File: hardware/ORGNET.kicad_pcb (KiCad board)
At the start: 2 copper layers, 21 x 50 mm, 3 parts, among them U3 AP2112K-3.3, U5 W25Q128JVP, U6 Raspberry Pi Radio Module 2

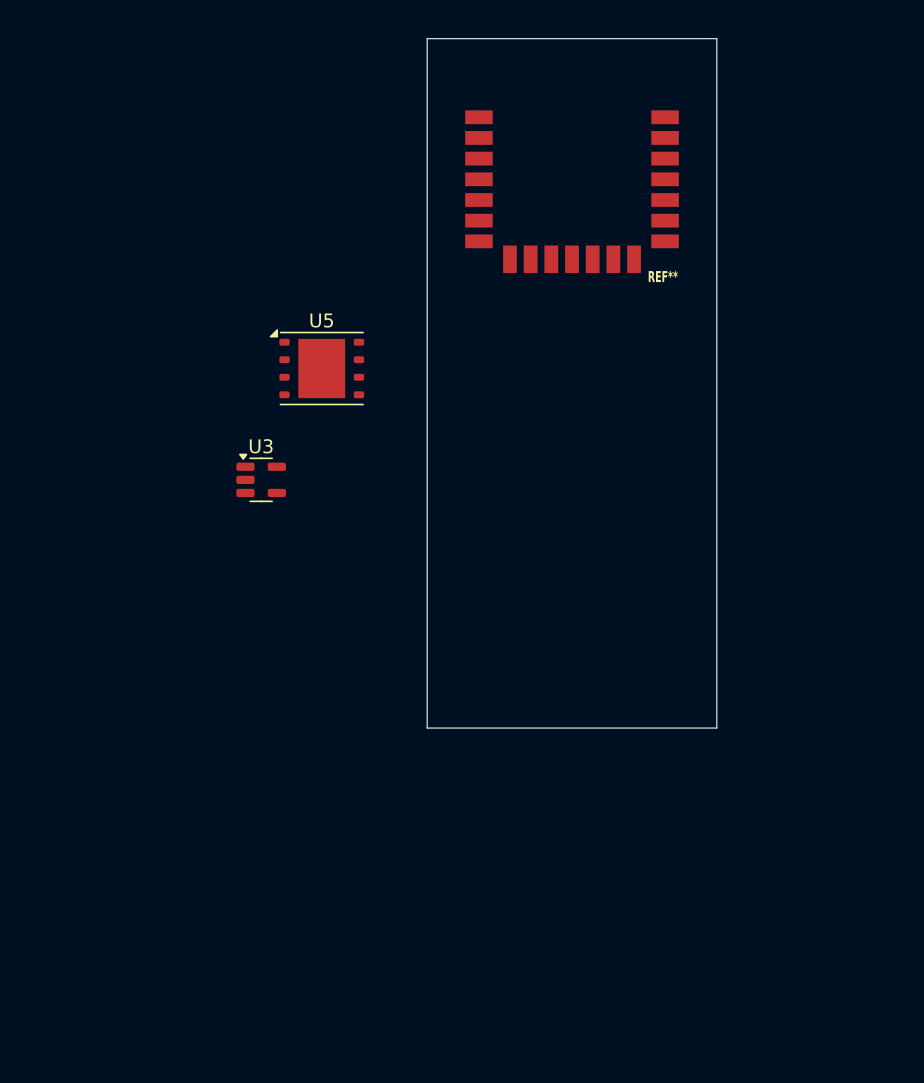
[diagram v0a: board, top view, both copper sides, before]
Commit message: Begin laying out footprints on PCB
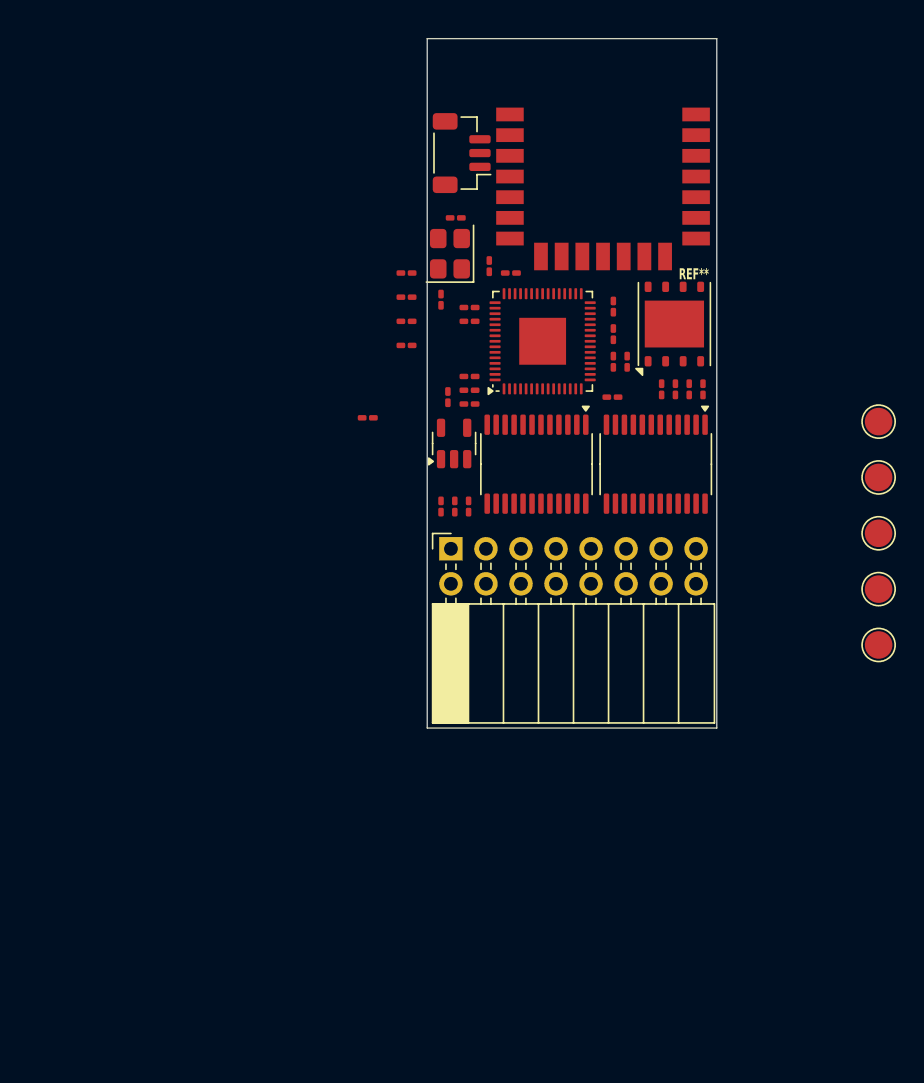
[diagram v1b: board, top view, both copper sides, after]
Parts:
- added C1: 0.1u, Capacitor_SMD:C_0201_0603Metric_Pad0.64x0.40mm_HandSolder, F.Cu at (188.0, 75.4)
- added C10: 0.1u, Capacitor_SMD:C_0201_0603Metric_Pad0.64x0.40mm_HandSolder, F.Cu at (174.1, 75.5)
- added C11: 0.1u, Capacitor_SMD:C_0201_0603Metric_Pad0.64x0.40mm_HandSolder, F.Cu at (184.5, 71.4)
- added C12: 0.1u, Capacitor_SMD:C_0201_0603Metric_Pad0.64x0.40mm_HandSolder, F.Cu at (184.5, 69.4)
- added C13: 1u, Capacitor_SMD:C_0201_0603Metric_Pad0.64x0.40mm_HandSolder, F.Cu at (177.1, 67.0)
- added C14: 1u, Capacitor_SMD:C_0201_0603Metric_Pad0.64x0.40mm_HandSolder, F.Cu at (175.5, 66.5)
- added C15: 1u, Capacitor_SMD:C_0201_0603Metric_Pad0.64x0.40mm_HandSolder, F.Cu at (174.1, 70.5)
- added C16: 1u, Capacitor_SMD:C_0201_0603Metric_Pad0.64x0.40mm_HandSolder, F.Cu at (174.1, 69.5)
- added C17: 0.1u, Capacitor_SMD:C_0201_0603Metric_Pad0.64x0.40mm_HandSolder, F.Cu at (174.1, 76.5)
- added C18: 15p, Capacitor_SMD:C_0201_0603Metric_Pad0.64x0.40mm_HandSolder, F.Cu at (173.1, 63.0)
- added C19: 15p, Capacitor_SMD:C_0201_0603Metric_Pad0.64x0.40mm_HandSolder, F.Cu at (172.0, 68.9)
- added C2: 1u, Capacitor_SMD:C_0201_0603Metric_Pad0.64x0.40mm_HandSolder, F.Cu at (174.0, 83.9)
- added C3: 0.1u, Capacitor_SMD:C_0201_0603Metric_Pad0.64x0.40mm_HandSolder, F.Cu at (173.0, 83.9)
- added C4: 0.1u, Capacitor_SMD:C_0201_0603Metric_Pad0.64x0.40mm_HandSolder, F.Cu at (191.0, 75.4)
- added C5: 1u, Capacitor_SMD:C_0201_0603Metric_Pad0.64x0.40mm_HandSolder, F.Cu at (189.0, 75.4)
- added C6: 0.1u, Capacitor_SMD:C_0201_0603Metric_Pad0.64x0.40mm_HandSolder, F.Cu at (190.0, 75.4)
- added C7: 1u, Capacitor_SMD:C_0201_0603Metric_Pad0.64x0.40mm_HandSolder, F.Cu at (172.0, 83.9)
- added C8: 1u, Capacitor_SMD:C_0201_0603Metric_Pad0.64x0.40mm_HandSolder, F.Cu at (172.5, 76.0)
- added C9: 0.1u, Capacitor_SMD:C_0201_0603Metric_Pad0.64x0.40mm_HandSolder, F.Cu at (174.1, 74.5)
- added J1: Conn_02x08_Odd_Even, Connector_PinSocket_2.54mm:PinSocket_2x08_P2.54mm_Horizontal, F.Cu at (172.7, 87.0)
- added J3: Conn_01x03, Connector_JST:JST_SH_BM03B-SRSS-TB_1x03-1MP_P1.00mm_Vertical, F.Cu at (173.5, 58.3)
- added R1: 10k, Resistor_SMD:R_0201_0603Metric_Pad0.64x0.40mm_HandSolder, F.Cu at (184.5, 73.4)
- added R2: 10k, Resistor_SMD:R_0201_0603Metric_Pad0.64x0.40mm_HandSolder, F.Cu at (184.4, 76.0)
- added R3: 10k, Resistor_SMD:R_0201_0603Metric_Pad0.64x0.40mm_HandSolder, F.Cu at (185.5, 73.4)
- added R4: 100k, Resistor_SMD:R_0201_0603Metric_Pad0.64x0.40mm_HandSolder, F.Cu at (166.7, 77.5)
- added R5: 100k, Resistor_SMD:R_0201_0603Metric_Pad0.64x0.40mm_HandSolder, F.Cu at (169.5, 67.0)
- added R6: 100k, Resistor_SMD:R_0201_0603Metric_Pad0.64x0.40mm_HandSolder, F.Cu at (169.5, 68.8)
- added R7: 470, Resistor_SMD:R_0201_0603Metric_Pad0.64x0.40mm_HandSolder, F.Cu at (169.5, 70.5)
- added R8: 10k, Resistor_SMD:R_0201_0603Metric_Pad0.64x0.40mm_HandSolder, F.Cu at (169.5, 72.2)
- added TP1: TestPoint, TestPoint:TestPoint_Pad_D2.0mm, F.Cu at (203.7, 77.8)
- added TP2: TestPoint, TestPoint:TestPoint_Pad_D2.0mm, F.Cu at (203.7, 81.8)
- added TP3: TestPoint, TestPoint:TestPoint_Pad_D2.0mm, F.Cu at (203.7, 85.9)
- added TP4: RESET, TestPoint:TestPoint_Pad_D2.0mm, F.Cu at (203.7, 89.9)
- added TP5: BOOTSEL, TestPoint:TestPoint_Pad_D2.0mm, F.Cu at (203.7, 94.0)
- added U1: SN74LVC8T245, Package_SO:TSSOP-24_4.4x7.8mm_P0.65mm, F.Cu at (178.9, 80.9)
- added U2: SN74LVC8T245, Package_SO:TSSOP-24_4.4x7.8mm_P0.65mm, F.Cu at (187.6, 80.9)
- added U4: RP2350A, Package_DFN_QFN:QFN-60-1EP_7x7mm_P0.4mm_EP3.4x3.4mm, F.Cu at (179.4, 72.0)
- added Y1: 12M, Crystal:Crystal_SMD_Abracon_ABM8G-4Pin_3.2x2.5mm, F.Cu at (172.7, 65.6)
- moved U5 25.8 mm to (188.9, 70.7), turned to 90 degrees
- moved U3 14.2 mm to (172.9, 79.4), turned to 90 degrees
- moved U6 2.26 mm to (183.8, 58.0)

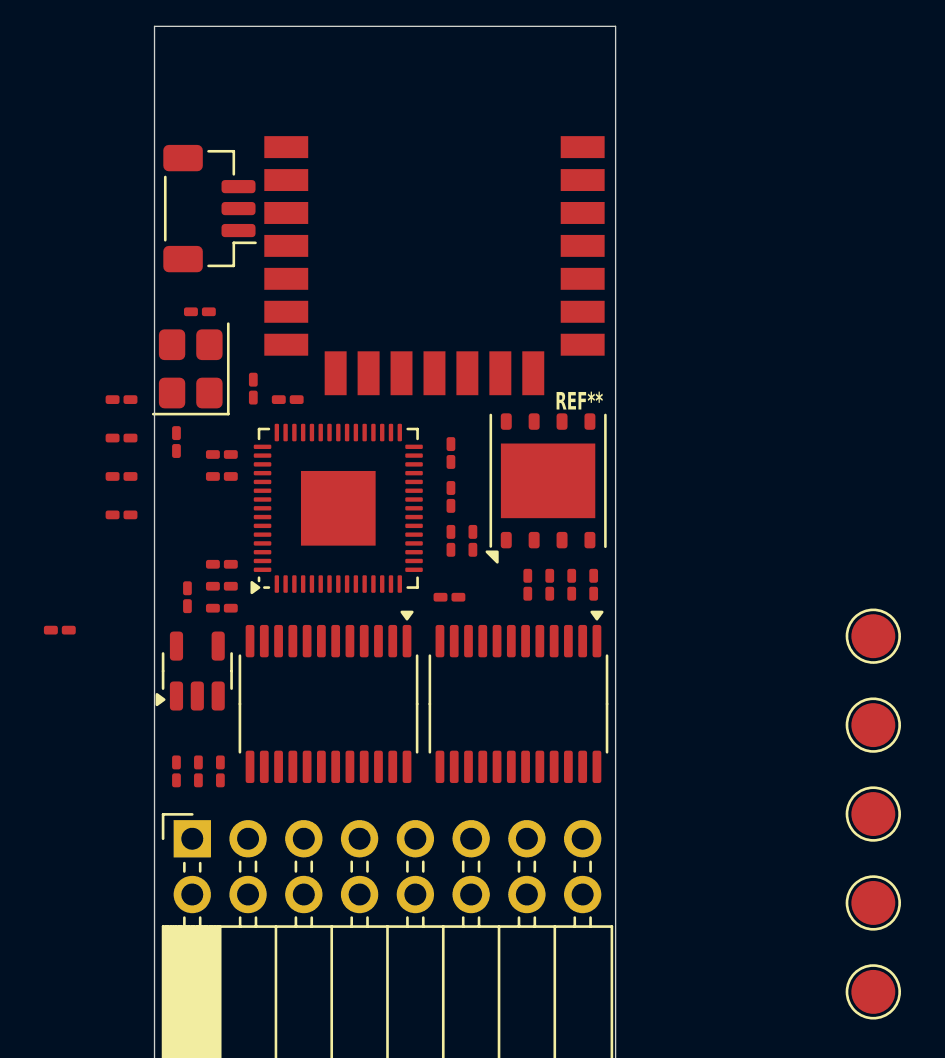
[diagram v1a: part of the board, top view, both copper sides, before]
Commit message: Start routing PCB
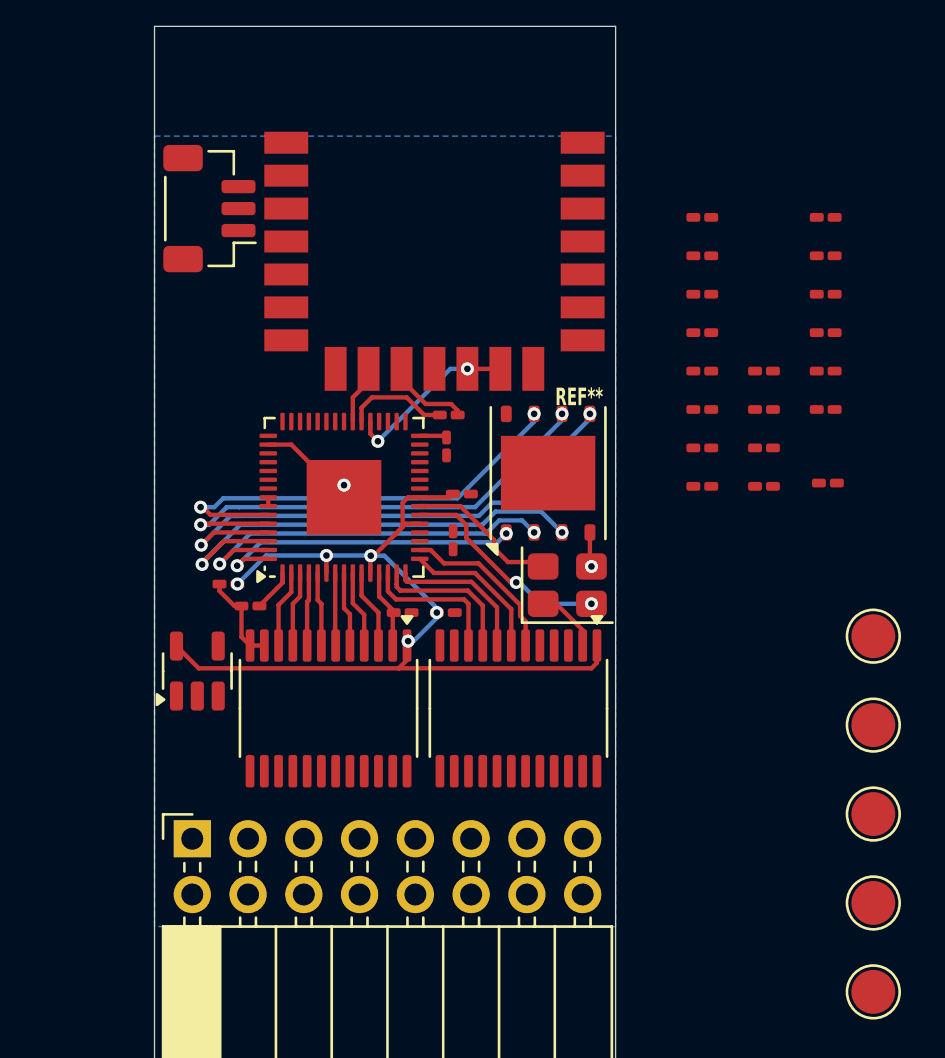
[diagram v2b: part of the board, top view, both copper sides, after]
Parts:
- moved R4 38.1 mm to (201.6, 62.2)
- moved R5 32.2 mm to (201.6, 64.0)
- moved R6 32.2 mm to (201.6, 65.7)
- moved R7 32.2 mm to (201.6, 67.5)
- moved C2 32.1 mm to (195.9, 60.5), turned to 0 degrees
- moved C3 31.6 mm to (195.9, 62.2), turned to 0 degrees
- moved C18 29.6 mm to (201.7, 70.8)
- moved C7 28.1 mm to (195.9, 69.2), turned to 0 degrees
- moved C19 26.8 mm to (198.8, 71.0), turned to 0 degrees
- moved C17 25.7 mm to (198.8, 69.2)
- moved C15 25.2 mm to (198.8, 65.7)
- moved C16 24.8 mm to (198.8, 67.5)
- moved C8 24.0 mm to (195.9, 71.0), turned to 0 degrees
- moved R1 22.5 mm to (201.6, 58.7), turned to 0 degrees
- moved R3 20.7 mm to (201.6, 60.5), turned to 0 degrees
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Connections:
- U2 pad 10: unconnected-(U2-A8-Pad10) -> RP_SMR
- U2 pad 14: GND -> SMR
- U2 pad 15: GND -> SCLK
- U2 pad 16: GND -> ~{SOE}
- U2 pad 17: SMR -> ~{SS}
- U2 pad 18: SCLK -> ~{SPGM}
- U2 pad 19: ~{SOE} -> GND
- U2 pad 20: ~{SS} -> GND
- U2 pad 21: ~{SPGM} -> GND
- U2 pad 3: ~{RP_SPGM} -> unconnected-(U2-A1-Pad3)
- U2 pad 4: ~{RP_SS} -> unconnected-(U2-A2-Pad4)
- U2 pad 5: ~{RP_SOE} -> unconnected-(U2-A3-Pad5)
- U2 pad 6: RP_SCLK -> ~{RP_SPGM}
- U2 pad 7: RP_SMR -> ~{RP_SS}
- U2 pad 8: unconnected-(U2-A6-Pad8) -> ~{RP_SOE}
- U2 pad 9: unconnected-(U2-A7-Pad9) -> RP_SCLK
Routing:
- net +3V3: track 0.00 -> 46.7 mm, vias 0 -> 5
- net Net-(U4-QSPI_SD0): track 0.00 -> 23.6 mm, vias 0 -> 2
- net Net-(U4-QSPI_SCLK): track 0.00 -> 21.8 mm, vias 0 -> 2
- net Net-(U4-QSPI_SD2): track 0.00 -> 21.3 mm, vias 0 -> 2
- net Net-(U4-QSPI_SD3): track 0.00 -> 20.4 mm, vias 0 -> 2
- net Net-(U4-QSPI_SD1): track 0.00 -> 17.8 mm, vias 0 -> 2
- net Net-(U4-~{QSPI_CS}): track 0.00 -> 14.4 mm, vias 0 -> 2
- net GND: track 0.00 -> 13.2 mm, vias 0 -> 2
- net Net-(U4-XIN): track 0.00 -> 9.84 mm, vias 0 -> 2
- net RM_ON: track 0.00 -> 7.99 mm, vias 0 -> 2
- net ~{RP_SPGM}: track 0.00 -> 7.56 mm
- net Net-(U4-XOUT): track 0.00 -> 6.98 mm
- net ~{RP_SS}: track 0.00 -> 6.77 mm
- net ~{RP_SOE}: track 0.00 -> 6.74 mm
- net RP_SCLK: track 0.00 -> 6.72 mm
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- added copper zone on B.Cu, net GND

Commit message: Finish off PCB routing
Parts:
- TP1, TP2, TP3, TP4, TP5: moved to B.Cu
- moved TP5 37.3 mm to (173.0, 72.9)
- moved TP1 34.0 mm to (173.0, 63.3)
- moved C2 33.1 mm to (172.6, 83.9)
- moved C3 32.4 mm to (172.6, 84.7)
- moved C1 32.4 mm to (173.9, 82.4), turned to -90 degrees
- moved R1 31.6 mm to (175.5, 76.5), turned to 180 degrees
- moved R5 31.0 mm to (172.4, 74.5)
- moved TP3 30.9 mm to (173.0, 82.4)
- moved TP2 30.9 mm to (173.0, 78.6)
- moved R6 28.8 mm to (174.5, 75.3)
- moved C5 28.4 mm to (172.6, 81.9), turned to 180 degrees
- moved C6 27.9 mm to (172.6, 82.7), turned to 180 degrees
- moved R7 26.8 mm to (175.2, 62.7), turned to 90 degrees
- moved C17 26.2 mm to (172.7, 66.5)
- moved C16 26.2 mm to (172.7, 65.6)
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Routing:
- net +3V3: track 46.7 -> 113.1 mm, vias 5 -> 11
- net SVCC: track 0.00 -> 61.6 mm, vias 0 -> 2
- net ~{OE}: track 0.00 -> 32.6 mm, vias 0 -> 4
- net DBG_SWDIO: track 0.00 -> 20.5 mm, vias 0 -> 2
- net GND: track 13.2 -> 32.1 mm, vias 2 -> 23
- net DBG_SWCLK: track 0.00 -> 18.1 mm, vias 0 -> 2
- net Net-(U4-QSPI_SD2): track 21.3 -> 4.10 mm, vias 2 -> 0
- net Net-(U4-QSPI_SD0): track 23.6 -> 6.84 mm, vias 2 -> 0
- net RM_DATA: track 4.72 -> 18.5 mm, vias 0 -> 3
- net Net-(U4-QSPI_SCLK): track 21.8 -> 8.73 mm, vias 2 -> 0
- net Net-(U4-QSPI_SD1): track 17.8 -> 5.53 mm, vias 2 -> 0
- net RM_SCLK: track 0.00 -> 12.2 mm
- net SD0: track 0.00 -> 10.4 mm, vias 0 -> 1
- net Net-(U4-QSPI_SD3): track 20.4 -> 10.1 mm, vias 2 -> 0
- net SD1: track 0.00 -> 9.74 mm, vias 0 -> 1
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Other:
- board text added: "3V3"
- board text added: "BSEL"
- board text added: "DBG"
- board text added: "GND"
- board text added: "RST"
- board text added: "SVCC"

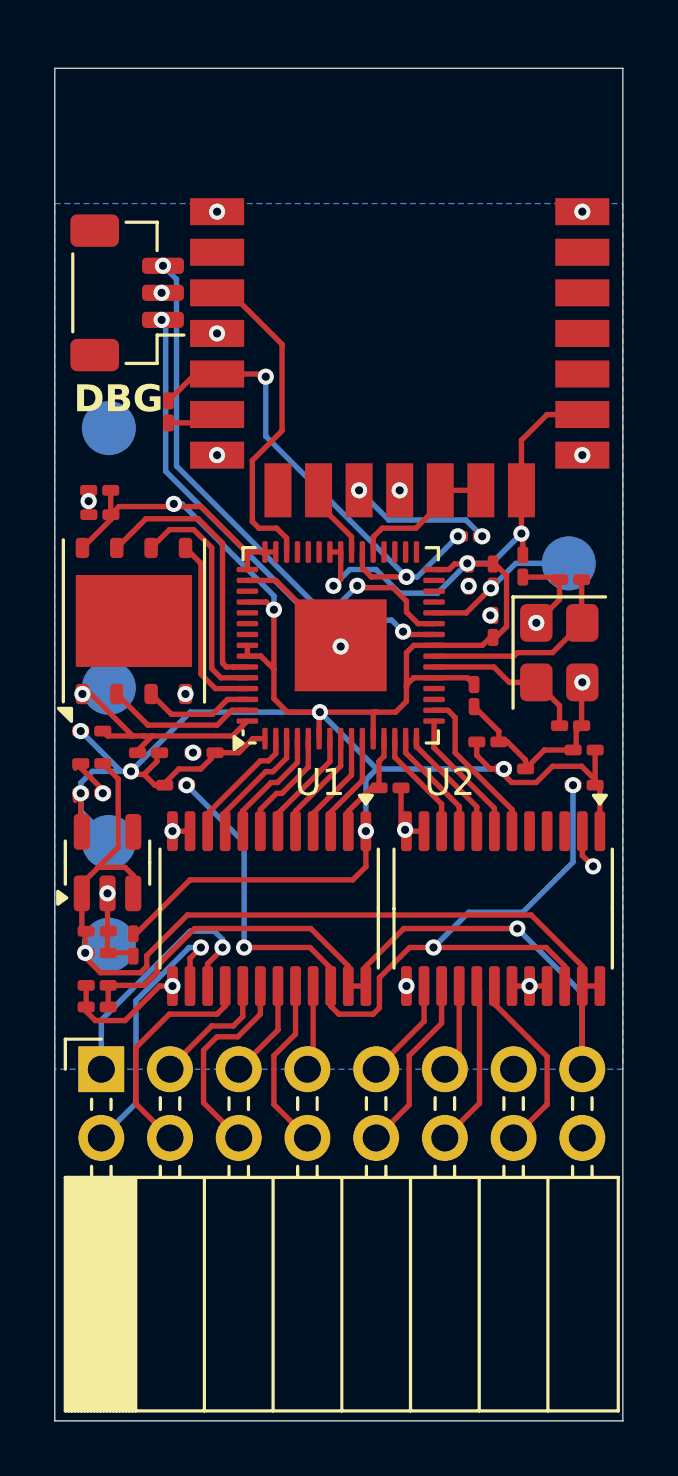
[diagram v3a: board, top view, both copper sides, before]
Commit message: Fix order of pins on connector
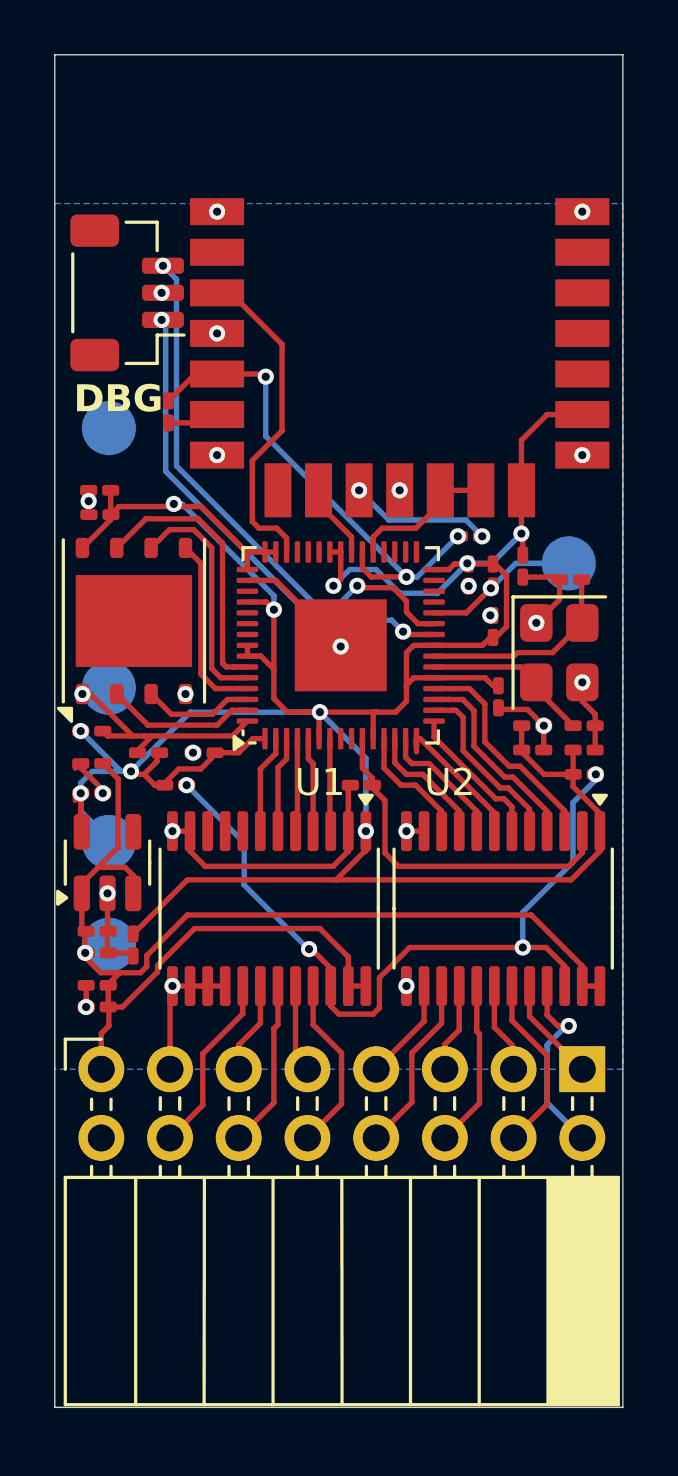
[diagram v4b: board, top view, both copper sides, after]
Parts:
- moved C11 1.77 mm to (188.7, 74.3)
- moved R2 1.06 mm to (182.3, 76.5), turned to 180 degrees
- moved C10 0.97 mm to (188.7, 75.2)
- moved C12 0.90 mm to (187.4, 73.2)
- moved C18 0.50 mm to (190.6, 74.3)
- moved R3 0.40 mm to (190.6, 76.1), turned to 180 degrees
- turned C4 to 0 degrees
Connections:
- U1 pad 10: RP_SD0 -> unconnected-(U1-A8-Pad10)
- U1 pad 14: SD0 -> GND
- U1 pad 15: SD1 -> GND
- U1 pad 16: SD2 -> GND
- U1 pad 17: SD3 -> ~{SPGM}
- U1 pad 18: SD4 -> ~{SOE}
- U1 pad 19: SD5 -> ~{SS}
- U1 pad 2: DIR -> GND
- U1 pad 20: SD6 -> SMR
- U1 pad 21: SD7 -> SCLK
- U1 pad 3: RP_SD7 -> RP_SCLK
- U1 pad 4: RP_SD6 -> RP_SMR
- U1 pad 5: RP_SD5 -> ~{RP_SS}
- U1 pad 6: RP_SD4 -> ~{RP_SOE}
- U1 pad 7: RP_SD3 -> ~{RP_SPGM}
- U1 pad 8: RP_SD2 -> unconnected-(U1-A6-Pad8)
- U1 pad 9: RP_SD1 -> unconnected-(U1-A7-Pad9)
- U2 pad 10: RP_SMR -> RP_SD7
- U2 pad 14: SMR -> SD7
- U2 pad 15: SCLK -> SD6
- U2 pad 16: ~{SOE} -> SD5
- U2 pad 17: ~{SS} -> SD4
- U2 pad 18: ~{SPGM} -> SD3
- U2 pad 19: GND -> SD2
- U2 pad 2: GND -> DIR
- U2 pad 20: GND -> SD1
- U2 pad 21: GND -> SD0
- U2 pad 3: unconnected-(U2-A1-Pad3) -> RP_SD0
- U2 pad 4: unconnected-(U2-A2-Pad4) -> RP_SD1
- U2 pad 5: unconnected-(U2-A3-Pad5) -> RP_SD2
- U2 pad 6: ~{RP_SPGM} -> RP_SD3
- U2 pad 7: ~{RP_SS} -> RP_SD4
- U2 pad 8: ~{RP_SOE} -> RP_SD5
- U2 pad 9: RP_SCLK -> RP_SD6
- U4 pad 10: RP_SD7 -> DIR
- U4 pad 12: DIR -> RP_SD7
- U4 pad 13: RP_SMR -> RP_SD6
- U4 pad 14: RP_SCLK -> RP_SD5
- U4 pad 15: ~{RP_SOE} -> RP_SD4
- U4 pad 16: ~{RP_SS} -> RP_SD3
- U4 pad 17: ~{RP_SPGM} -> RP_SD2
- U4 pad 18: unconnected-(U4-GPIO14-Pad18) -> RP_SD1
- U4 pad 19: unconnected-(U4-GPIO15-Pad19) -> RP_SD0
- U4 pad 2: RP_SD0 -> ~{RP_SPGM}
- U4 pad 3: RP_SD1 -> ~{RP_SOE}
- U4 pad 4: RP_SD2 -> ~{RP_SS}
- U4 pad 5: RP_SD3 -> RP_SMR
- U4 pad 7: RP_SD4 -> RP_SCLK
- U4 pad 8: RP_SD5 -> unconnected-(U4-GPIO5-Pad8)
- U4 pad 9: RP_SD6 -> unconnected-(U4-GPIO6-Pad9)
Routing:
- net SVCC: track 61.6 -> 49.1 mm, vias 2 -> 1
- net DIR: track 4.13 -> 13.1 mm
- net SD1: track 9.74 -> 3.28 mm, vias 1 -> 0
- net +3V3: track 113.1 -> 117.8 mm, vias 11 -> 10
- net GND: track 32.1 -> 35.9 mm
- net RP_SD0: track 4.64 -> 8.27 mm
- net SD0: track 10.4 -> 7.11 mm
- net ~{OE}: track 32.6 -> 29.7 mm
- net RP_SD1: track 4.52 -> 7.40 mm
- net ~{RP_SPGM}: track 5.96 -> 3.66 mm
- net RP_SD2: track 4.39 -> 6.58 mm
- net SD2: track 8.54 -> 6.80 mm
- net RP_SD4: track 4.24 -> 5.80 mm
- net ~{RP_SS}: track 4.99 -> 3.45 mm
- net SD3: track 4.66 -> 3.37 mm
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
